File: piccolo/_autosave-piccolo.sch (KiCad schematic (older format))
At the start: 2 parts

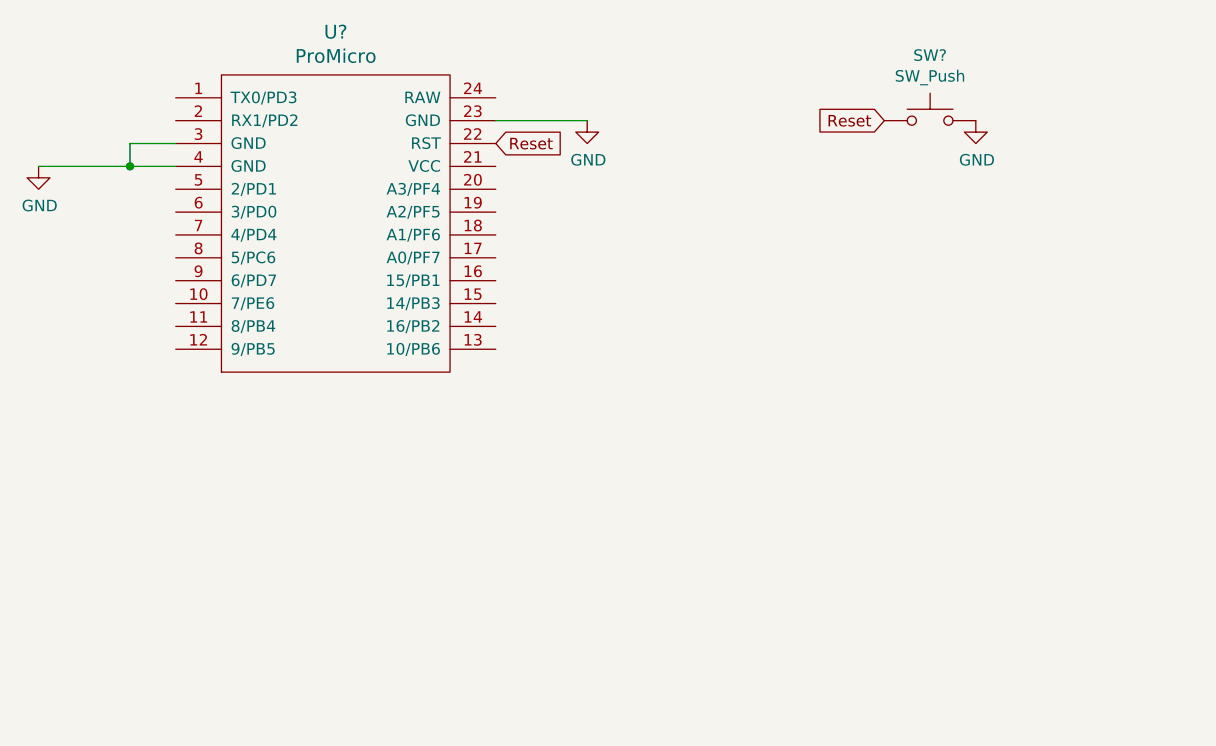
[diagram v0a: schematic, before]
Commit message: More kicad libs
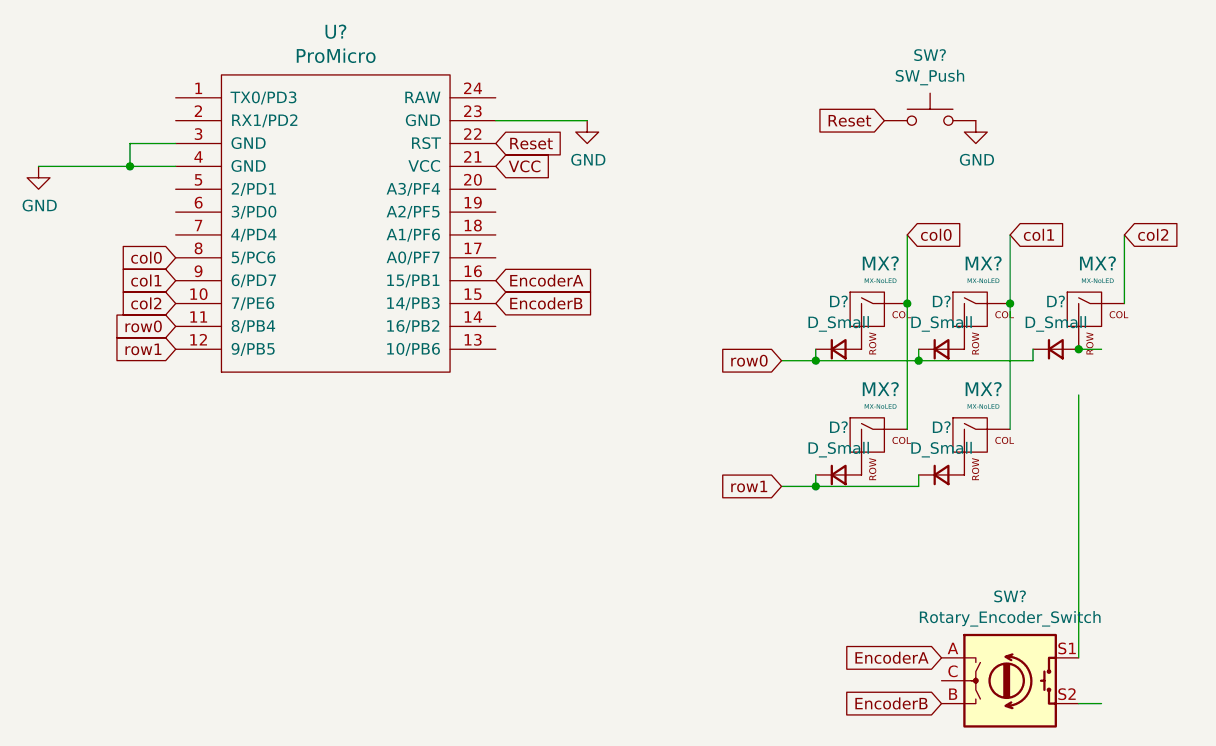
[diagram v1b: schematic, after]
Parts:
- added D? (x5): D_Small, symbol Device:D_Small
- added MX? (x5): MX-NoLED, symbol MX_Alps_Hybrid:MX-NoLED
- added SW?: Rotary_Encoder_Switch, symbol Device:Rotary_Encoder_Switch
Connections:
- net labels added: EncoderA, EncoderB, VCC, col0, col1, col2, row0, row1
- wire segments 5 -> 23
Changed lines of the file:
@@
 	1    0    0    -1
 $EndComp
+Text GLabel 3050 1950 2    50   Input ~ 0
+VCC
+$Comp
+L MX_Alps_Hybrid:MX-NoLED MX?
+U 1 1 614F0E12
+P 4700 2600
+F 0 "MX?" H 4733 2823 60  0000 C CNN
+F 1 "MX-NoLED" H 4733 2749 20  0000 C CNN
+F 2 "" H 4075 2575 60  0001 C CNN
+F 3 "" H 4075 2575 60  0001 C CNN
+	1    4700 2600
+	1    0    0    -1
+$EndComp
+$Comp
+L MX_Alps_Hybrid:MX-NoLED MX?
+U 1 1 614F1B4A
+P 5150 2600
+F 0 "MX?" H 5183 2823 60  0000 C CNN
+F 1 "MX-NoLED" H 5183 2749 20  0000 C CNN
+F 2 "" H 4525 2575 60  0001 C CNN
+F 3 "" H 4525 2575 60  0001 C CNN
+	1    5150 2600
+	1    0    0    -1
+$EndComp
+$Comp
+L MX_Alps_Hybrid:MX-NoLED MX?
+U 1 1 614F1EEE
+P 4700 3150
+F 0 "MX?" H 4733 3373 60  0000 C CNN
+F 1 "MX-NoLED" H 4733 3299 20  0000 C CNN
+F 2 "" H 4075 3125 60  0001 C CNN
+F 3 "" H 4075 3125 60  0001 C CNN
+	1    4700 3150
+	1    0    0    -1
+$EndComp
+$Comp
+L MX_Alps_Hybrid:MX-NoLED MX?
+U 1 1 614F33D1
+P 5150 3150
+F 0 "MX?" H 5183 3373 60  0000 C CNN
+F 1 "MX-NoLED" H 5183 3299 20  0000 C CNN
+F 2 "" H 4525 3125 60  0001 C CNN
+F 3 "" H 4525 3125 60  0001 C CNN
+	1    5150 3150
+	1    0    0    -1
+$EndComp
+$Comp
+L Device:D_Small D?
+U 1 1 614F574A
+P 4550 2750
+F 0 "D?" H 4550 2957 50  0000 C CNN
+F 1 "D_Small" H 4550 2866 50  0000 C CNN
+F 2 "" V 4550 2750 50  0001 C CNN
+F 3 "~" V 4550 2750 50  0001 C CNN
+	1    4550 2750
+	1    0    0    -1
+$EndComp
+$Comp
+L Device:D_Small D?
+U 1 1 614F66DB
+P 5000 2750
+F 0 "D?" H 5000 2957 50  0000 C CNN
+F 1 "D_Small" H 5000 2866 50  0000 C CNN
+F 2 "" V 5000 2750 50  0001 C CNN
+F 3 "~" V 5000 2750 50  0001 C CNN
+	1    5000 2750
+	1    0    0    -1
+$EndComp
+$Comp
+L Device:D_Small D?
+U 1 1 614F6C0A
+P 4550 3300
+F 0 "D?" H 4550 3507 50  0000 C CNN
+F 1 "D_Small" H 4550 3416 50  0000 C CNN
+F 2 "" V 4550 3300 50  0001 C CNN
+F 3 "~" V 4550 3300 50  0001 C CNN
+	1    4550 3300
+	1    0    0    -1
+$EndComp
+$Comp
+L Device:D_Small D?
+U 1 1 614F770C
+P 5000 3300
+F 0 "D?" H 5000 3507 50  0000 C CNN
+F 1 "D_Small" H 5000 3416 50  0000 C CNN
+F 2 "" V 5000 3300 50  0001 C CNN
+F 3 "~" V 5000 3300 50  0001 C CNN
+	1    5000 3300
+	1    0    0    -1
+$EndComp
+Wire Wire Line
+	4850 2550 4850 3100
+Wire Wire Line
+	5300 2550 5300 3100
+Wire Wire Line
+	5300 2550 5300 2250
+Connection ~ 5300 2550
+Wire Wire Line
+	4850 2550 4850 2250
+Connection ~ 4850 2550
+Wire Wire Line
+	4900 2750 4900 2800
+Wire Wire Line
+	4900 2800 4450 2800
+Wire Wire Line
+	4450 2800 4450 2750
+Wire Wire Line
+	4450 2800 4300 2800
+Connection ~ 4450 2800
+Wire Wire Line
+	4900 3300 4900 3350
+Wire Wire Line
+	4900 3350 4450 3350
+Wire Wire Line
+	4450 3350 4450 3300
+Wire Wire Line
+	4450 3350 4300 3350
+Connection ~ 4450 3350
+Text GLabel 4850 2250 2    50   Input ~ 0
+col0
+Text GLabel 5300 2250 2    50   Input ~ 0
+col1
+Text GLabel 4300 2800 0    50   Input ~ 0
+row0
+Text GLabel 4300 3350 0    50   Input ~ 0
+row1
+$Comp
+L MX_Alps_Hybrid:MX-NoLED MX?
+U 1 1 614FC81C
+P 5650 2600
+F 0 "MX?" H 5683 2823 60  0000 C CNN
+F 1 "MX-NoLED" H 5683 2749 20  0000 C CNN
+F 2 "" H 5025 2575 60  0001 C CNN
+F 3 "" H 5025 2575 60  0001 C CNN
+	1    5650 2600
+	1    0    0    -1
+$EndComp
+$Comp
+L Device:D_Small D?
+U 1 1 614FCDC3
+P 5500 2750
+F 0 "D?" H 5500 2957 50  0000 C CNN
+F 1 "D_Small" H 5500 2866 50  0000 C CNN
+F 2 "" V 5500 2750 50  0001 C CNN
+F 3 "~" V 5500 2750 50  0001 C CNN
+	1    5500 2750
+	1    0    0    -1
+$EndComp
+Wire Wire Line
+	5400 2750 5400 2800
+Wire Wire Line
+	5400 2800 4900 2800
+Connection ~ 4900 2800
+Wire Wire Line
+	5800 2550 5800 2250
+Text GLabel 5800 2250 2    50   Input ~ 0
+col2
+Text GLabel 1650 2650 0    50   Input ~ 0
+row0
+Text GLabel 1650 2750 0    50   Input ~ 0
+row1
+Text GLabel 1650 2350 0    50   Input ~ 0
+col0
+Text GLabel 1650 2450 0    50   Input ~ 0
+col1
+Text GLabel 1650 2550 0    50   Input ~ 0
+col2
+$Comp
+L Device:Rotary_Encoder_Switch SW?
+U 1 1 6150121A
+P 5300 4200
+F 0 "SW?" H 5300 4567 50  0000 C CNN
+F 1 "Rotary_Encoder_Switch" H 5300 4476 50  0000 C CNN
+F 2 "" H 5150 4360 50  0001 C CNN
+F 3 "~" H 5300 4460 50  0001 C CNN
+	1    5300 4200
+	1    0    0    -1
+$EndComp
+Text GLabel 5000 4100 0    50   Input ~ 0
+EncoderA
+Text GLabel 5000 4300 0    50   Input ~ 0
+EncoderB
+Text GLabel 3050 2450 2    50   Input ~ 0
+EncoderA
+Text GLabel 3050 2550 2    50   Input ~ 0
+EncoderB
+Wire Wire Line
+	5600 4100 5600 2950
+Connection ~ 5600 2750
+Wire Wire Line
+	5600 4300 5700 4300
+Wire Wire Line
+	5700 2750 5600 2750
 $EndSCHEMATC
